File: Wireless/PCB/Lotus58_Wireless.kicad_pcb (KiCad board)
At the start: 2 copper layers, 139.1 x 107.7 mm, 122 parts, among them J1 AudioJack4, P4 OLED, SW1 SW_PUSH, SW10 SW_PUSH, SW11 SW_PUSH, SW12 SW_PUSH, SW13 SW_PUSH, SW14 SW_PUSH, SW15 SW_PUSH, SW16 SW_PUSH, SW17 SW_PUSH, SW18 SW_PUSH, SW19 SW_PUSH, SW2 SW_PUSH, SW20 SW_PUSH, SW21 SW_PUSH, SW22 SW_PUSH, SW23 SW_PUSH, SW24 SW_PUSH, SW25 SW_PUSH, SW26 SW_PUSH, SW27 SW_PUSH, SW28 SW_PUSH, SW29 SW_PUSH, SW3 SW_PUSH, SW30 Rotary_Encoder_Switch, SW31 Rotary_Encoder_Switch, SW4 SW_PUSH, SW5 SW_PUSH, SW6 SW_PUSH, SW7 SW_PUSH, SW8 SW_PUSH, SW9 SW_PUSH, U1 ProMicro

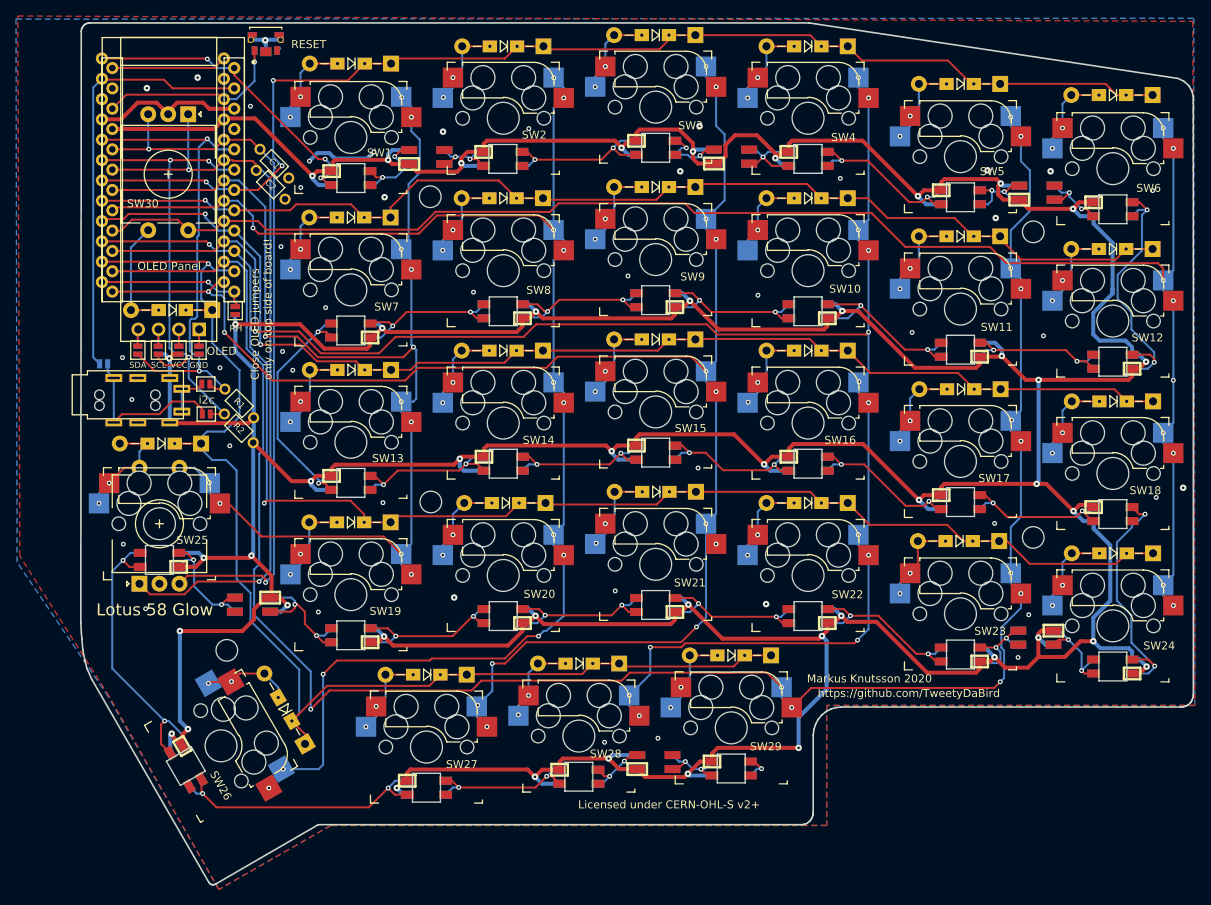
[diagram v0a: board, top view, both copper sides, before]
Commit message: RGB midmount footprints
Fixed mirror image pinout
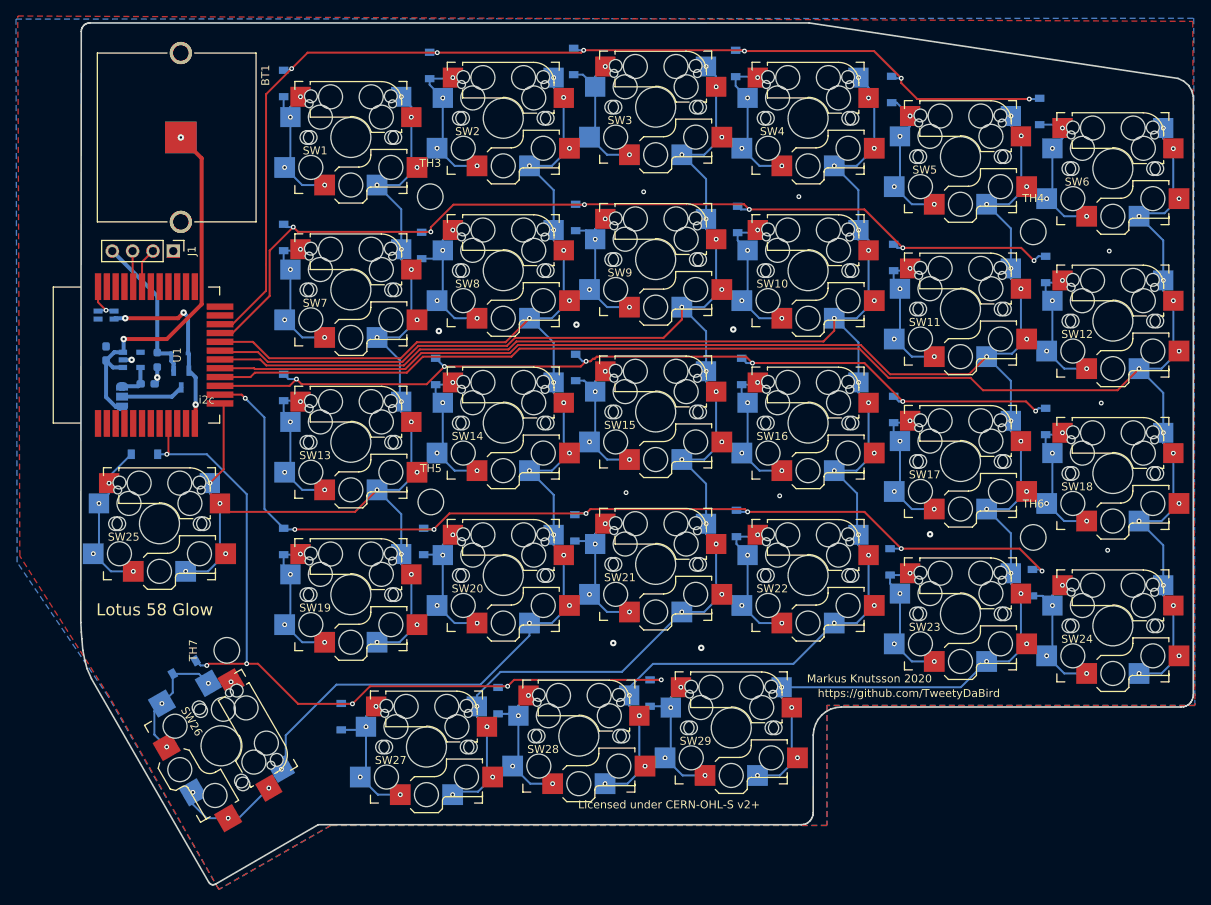
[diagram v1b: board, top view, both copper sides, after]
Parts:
- removed JP10, JP11, JP2, JP3, JP4, JP5, JP6, JP7, JP8, JP9: Jumper_NO_Small, Keyboard Library:Jumper_Mini
- removed L1, L10, L11, L12, L13, L14, L15, L16, L17, L18, L19, L2, L20, L21, L22, L23, L24, L25, L26, L27, L28, L29, L3, L4, L5, L6, L7, L8, L9: SK6812mini, Keyboard Library:SK6812MINI_Midmount_Reversible
- removed L30, L31, L32, L33, L34, L35: SK6812mini, Keyboard Library:SK6812MINI_Reversible
- removed P4: OLED, KiCad-SSD1306-0.91-OLED-4pin-128x32:SSD1306-0.91-OLED-4pin-128x32
- removed R2: R, Keyboard Library:RESISTOR_Reversible
- removed RESET: EVP-AKE31A, Keyboard Library:Panasonic-EVP-AKE31A-MFG_reversible
- removed SW30, SW31: Rotary_Encoder_Switch, Keebio-Parts:RotaryEncoder_EC11-no-legs
- added BT1: Battery_Cell, Keyboard Library:BAT_BK-888, F.Cu at (93.2, 50.0)
- added BT2: Battery_Cell, Keyboard Library:BAT_BK-888, B.Cu at (93.2, 50.0)
- added Q1: SI2393DS-T1-GE3, SamacSys_Parts:SOT95P237X112-3N, B.Cu at (93.2, 80.2)
- added U2: MCP1802x-xx02xOT, Package_TO_SOT_SMD:SOT-23-5, B.Cu at (87.0, 77.8)
- C1, C2: value C_Small -> 1uF; footprint Keyboard Library:RESISTOR_Reversible -> Capacitor_SMD:C_0603_1608Metric_Pad1.05x0.95mm_HandSolder
- D1, D10, D11, D12, D13, D14, D15, D16, D17, D18, D19, D2, D20, D21, D22, D23, D24, D25, D26, D27, D28, D29, D3, D4, D5, D6, D7, D8, D9: value D -> 1N4148W; footprint Keyboard Library:Diode_DO35_SOD123 -> Diode_SMD:D_SOD-123
- D30: value D -> BAT60A; footprint Keyboard Library:Diode_DO35_SOD123 -> Diode_SMD:D_SOD-323; moved to B.Cu
- J1: value AudioJack4 -> Conn_01x04; footprint Keyboard Library:MJ-4PP-9_alim -> Connector_PinHeader_2.54mm:PinHeader_1x04_P2.54mm_Vertical
- JP1: value Jumper_NO_Small -> Jumper_3_Open; footprint Keyboard Library:Jumper_Mini -> Jumper:SolderJumper-3_P1.3mm_Open_RoundedPad1.0x1.5mm; moved to B.Cu
- JP13: moved to B.Cu
- R1: value R -> 3k3; footprint Keyboard Library:RESISTOR_Reversible -> Resistor_SMD:R_0603_1608Metric_Pad0.98x0.95mm_HandSolder; moved to B.Cu
- SW1, SW10, SW11, SW12, SW13, SW14, SW15, SW16, SW17, SW18, SW19, SW2, SW20, SW21, SW22, SW23, SW24, SW25, SW26, SW27, SW28, SW29, SW3, SW4, SW5, SW6, SW7, SW8, SW9: footprint keyswitches:Kailh_socket_MX_reversible_RGB -> keyswitches:Kaih_socket_MX_Choc_V1&V2_reversible
- TH3, TH4, TH5, TH6, TH7: footprint MountingHole:MountingHole_2.7mm_M2.5 -> MountingHole:MountingHole_3.2mm_M3
- U1: value ProMicro -> Core51822B; footprint Keyboard Library:ProMicro_Reversible -> Keyboard Library:Core51822(B)_y14015
- moved C1 31.7 mm to (83.8, 77.0), turned to 90 degrees
- moved C2 29.3 mm to (89.0, 80.8), turned to 0 degrees
- moved U1 22.8 mm to (87.6, 77.2), turned to 90 degrees
- moved J1 20.9 mm to (92.2, 64.2), turned to 270 degrees
- moved JP13 17.2 mm to (82.8, 72.2)
- moved JP12 15.2 mm to (84.8, 72.2)
- moved D26 13.7 mm to (93.6, 116.2), turned to 210 degrees
- moved D27 11.9 mm to (113.2, 122.4), turned to 270 degrees
- moved D8 11.8 mm to (123.2, 63.5), turned to 270 degrees
- moved R1 11.6 mm to (90.2, 77.8), turned to 270 degrees
- moved D20 11.3 mm to (123.5, 100.5), turned to 270 degrees
- moved JP1 11.2 mm to (85.8, 82.4), turned to 90 degrees
- moved D29 11.2 mm to (151.8, 119.5), turned to 270 degrees
- moved D28 11.1 mm to (132.8, 120.4), turned to 270 degrees
- moved D21 11.1 mm to (142.4, 98.8), turned to 270 degrees
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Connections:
- net Alt renamed Net-(D25-Pad2)
- C1 pad 1: B -> +BATT
- C2 pad 1: GND -> +3V3
- C2 pad 2: A -> GND
- D30 pad 1: row4 -> VCC
- D30 pad 2: Net-(D30-Pad2) -> VPP
- JP1 pad 1: Net-(JP1-Pad1) -> +BATT
- JP1 pad 2: GND -> /POWER
- R1 pad 1: VCC -> VPP
- R1 pad 2: SDA -> GND
- U1 pad 1: LED -> GND
- U1 pad 10: row3 -> (no net)
- U1 pad 11: row4 -> GND
- U1 pad 12: Hand -> VCC
- U1 pad 13: col3 -> col5
- U1 pad 14: col1 -> row3
- U1 pad 15: col2 -> row2
- U1 pad 17: col4 -> col1
- U1 pad 18: col5 -> col2
- U1 pad 19: A -> col3
- U1 pad 2: DATA -> (no net)
- U1 pad 20: B -> col4
- U1 pad 21: VCC -> row1
- U1 pad 22: RESET -> row0
- U1 pad 23: GND -> (no net)
- U1 pad 24: Net-(U1-Pad24) -> (no net)
- U1 pad 3: GND -> (no net)
- U1 pad 4: GND -> (no net)
- U1 pad 5: SDA -> (no net)
- U1 pad 6: SCL -> (no net)
- U1 pad 7: row0 -> (no net)
- U1 pad 8: row1 -> (no net)
- U1 pad 9: row2 -> row4
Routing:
- net VCC: track 843.5 -> 24.0 mm, vias 45 -> 3
- net A: track 95.3 -> 0.00 mm, vias 2 -> 0
- net B: track 90.9 -> 0.00 mm, vias 2 -> 0
- net SDA: track 63.1 -> 0.00 mm, vias 2 -> 0
- net SCL: track 59.3 -> 0.00 mm, vias 3 -> 0
- net row4: track 160.0 -> 103.8 mm, vias 1 -> 6
- net DATA: track 53.4 -> 0.00 mm
- net +BATT: track 0.00 -> 47.2 mm, vias 0 -> 2
- net row3: track 169.3 -> 127.4 mm, vias 2 -> 7
- net LED: track 39.0 -> 0.00 mm, vias 3 -> 0
- net Net-(L25-Pad1): track 37.4 -> 0.00 mm, vias 2 -> 0
- net row2: track 151.3 -> 115.8 mm, vias 2 -> 6
- net Net-(L26-Pad1): track 34.3 -> 0.00 mm, vias 2 -> 0
- net Net-(L12-Pad3): track 33.5 -> 0.00 mm, vias 2 -> 0
- net GND: track 35.3 -> 3.32 mm, vias 45 -> 15
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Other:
- board text removed: "Close OLED jumpers only on top side of board!"
- board text removed: "OLED"
- board text removed: "Serial"
